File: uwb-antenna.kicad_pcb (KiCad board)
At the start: 2 copper layers, 53 parts, among them J1 USB C, J2 Battery, J3 SWD, SW1 ~{PB}, SW2 BOOT0, SW4 ~{SR}, U1 STM6600, U2 BQ24074RGT, U3 TPS63001, U5 STM32L432KBUx

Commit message: start placing some components in PCB design
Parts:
- removed D6: LTST-C235KGKRKT, LED_SMD:LED_LiteOn_LTST-C235KGKRKT
- removed J3: SWD, Connector_PinHeader_2.54mm:PinHeader_1x04_P2.54mm_Vertical
- added C3: 0.1uF, Capacitor_SMD:C_0402_1005Metric, F.Cu at (91.7, 117.5)
- added D7: LED_Dual_AAKK, LED_SMD:LED_LiteOn_LTST-C295K_1.6x0.8mm, F.Cu at (172.7, 84.5)
- added H1: MH1, MountingHole:MountingHole_3.2mm_M3_Pad, F.Cu at (140.9, 123.9)
- added H2: MH2, MountingHole:MountingHole_3.2mm_M3_Pad, F.Cu at (174.9, 123.9)
- added H3: MH3, MountingHole:MountingHole_3.2mm_M3_Pad, F.Cu at (174.9, 64.9)
- added H4: MH4, MountingHole:MountingHole_3.2mm_M3_Pad, F.Cu at (140.9, 64.9)
- added J4: Conn_ST_STDC14, Connector_PinHeader_1.27mm:PinHeader_2x07_P1.27mm_Vertical_SMD, F.Cu at (173.1, 92.1)
- J2: footprint BH-18650-PC:BAT_BH-18650-PC -> Connector_JST:JST_PH_S2B-PH-SM4-TB_1x02-1MP_P2.00mm_Horizontal
- R17, R6: footprint Resistor_SMD:R_0805_2012Metric -> Resistor_SMD:R_0402_1005Metric
- moved DWM1 58.7 mm to (157.9, 74.7)
- moved D1 56.4 mm to (115.6, 109.4)
- moved R17 53.4 mm to (175.1, 85.0)
- moved R12 53.0 mm to (92.0, 92.6)
- moved R13 53.0 mm to (92.0, 94.6)
- moved R15 53.0 mm to (92.0, 96.6)
- moved R16 53.0 mm to (92.0, 98.6)
- moved U1 53.0 mm to (112.3, 94.0)
- moved C1 53.0 mm to (74.5, 102.6)
- moved C2 53.0 mm to (74.5, 104.6)
- moved C4 53.0 mm to (74.5, 106.5)
- moved C5 53.0 mm to (74.5, 108.5)
- moved C7 53.0 mm to (74.5, 110.5)
- moved D2 53.0 mm to (86.4, 100.6)
- moved D3 53.0 mm to (86.4, 102.6)
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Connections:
- U5 pad 26: /~{CE} -> /SWO
- U5 pad 27: unconnected-(U5-PB4-Pad27) -> /~{CE}
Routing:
- added copper zone on F.Cu, net GND
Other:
- board outline added: 40 x 68 mm

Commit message: feat: place other components in the PCB
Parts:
- added C18: 4.7uF, Capacitor_SMD:C_0805_2012Metric, F.Cu at (166.6, 101.5)
- C7: footprint Capacitor_SMD:C_0402_1005Metric -> Capacitor_SMD:C_0805_2012Metric
- moved C7 88.4 mm to (162.7, 106.4)
- moved R1 83.9 mm to (164.3, 123.1), turned to 90 degrees
- moved R9 77.3 mm to (165.9, 103.1)
- moved R10 77.2 mm to (165.9, 104.4)
- moved R12 75.2 mm to (165.9, 106.4)
- moved R2 71.4 mm to (151.6, 123.1), turned to 90 degrees
- moved R11 70.5 mm to (159.4, 104.0), turned to -90 degrees
- moved U2 67.3 mm to (162.6, 101.7), turned to 180 degrees
- moved C8 63.3 mm to (158.9, 100.7), turned to 90 degrees
- moved FB1 59.9 mm to (154.4, 118.1), turned to 90 degrees
- moved D1 43.1 mm to (157.9, 117.7), turned to -90 degrees
- moved C3 11.5 mm to (84.1, 108.8)
- moved C9 10.8 mm to (164.8, 119.0), turned to 0 degrees
- moved R14 10.5 mm to (162.3, 119.0), turned to 0 degrees
- moved U5 9.16 mm to (144.4, 107.4)
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
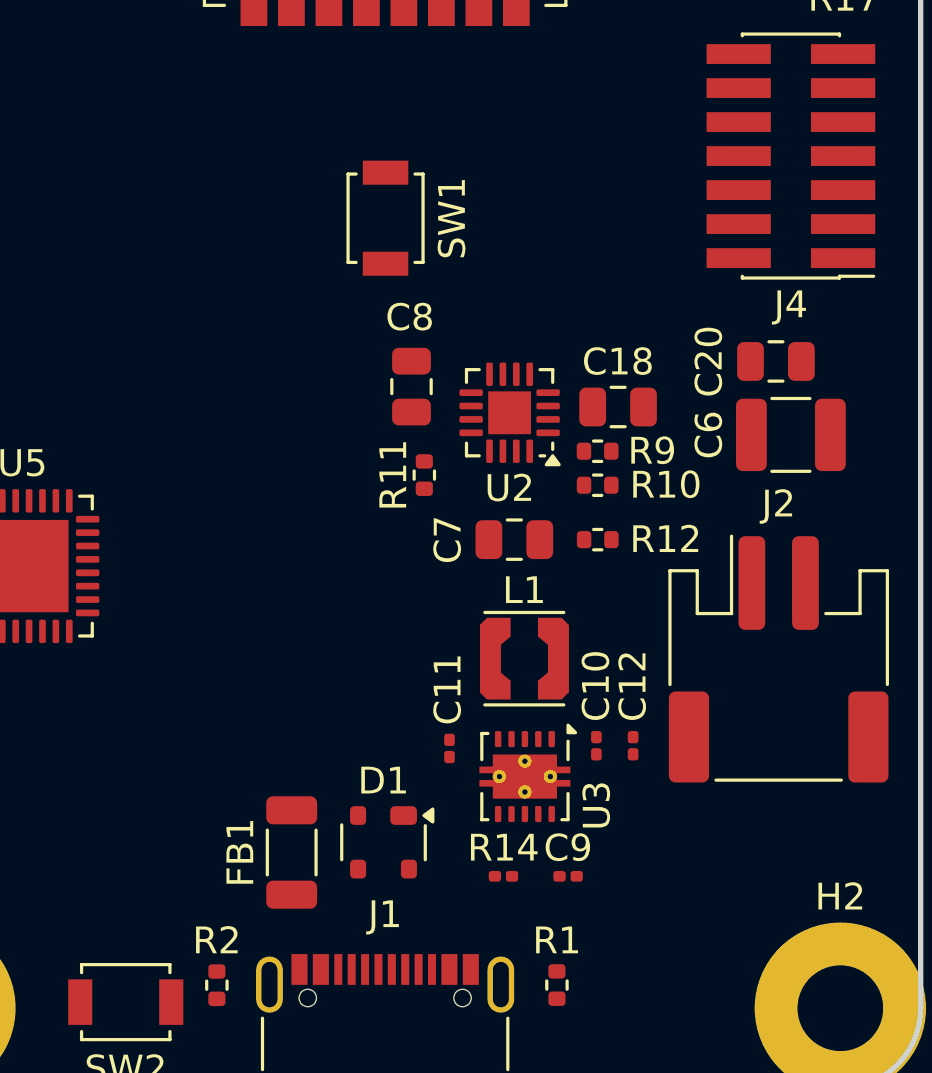
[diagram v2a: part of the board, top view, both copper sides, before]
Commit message: add battery filled zone
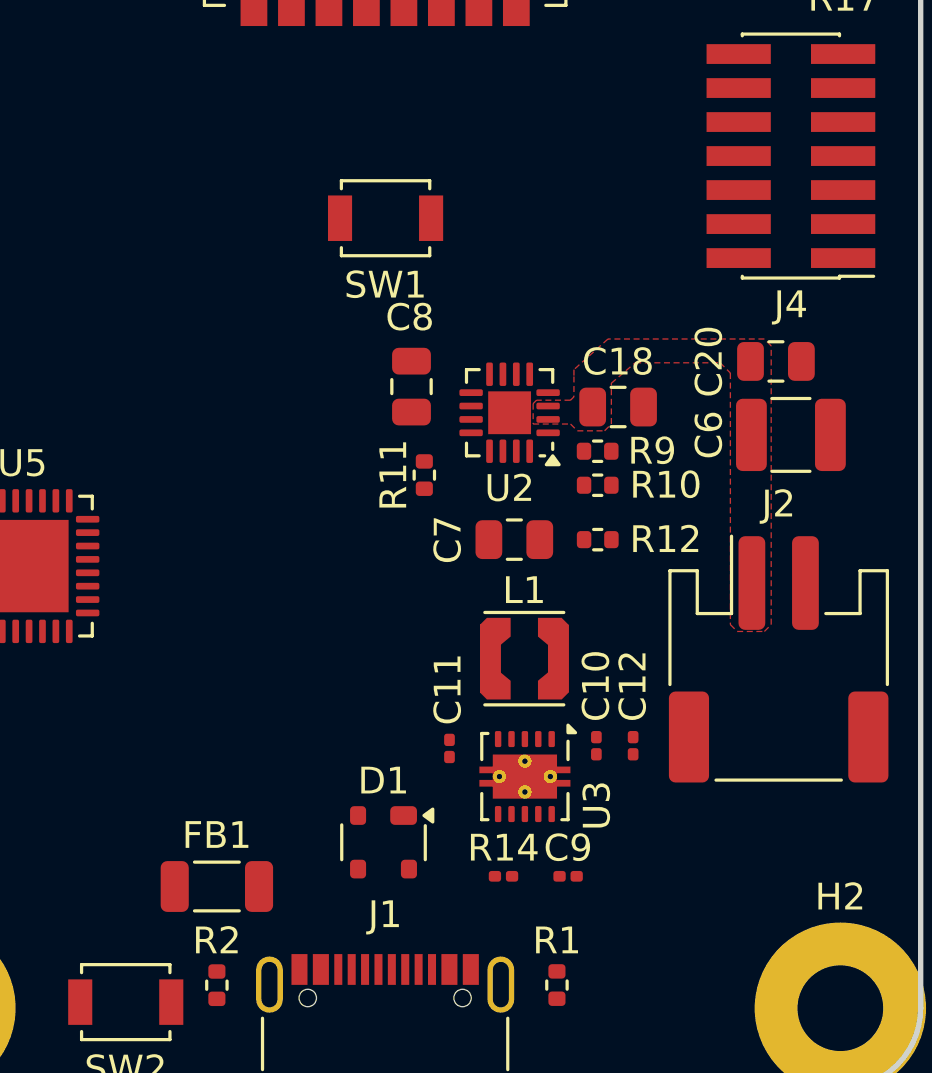
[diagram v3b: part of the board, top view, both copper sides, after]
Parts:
- moved FB1 3.07 mm to (151.6, 119.4), turned to 180 degrees
- turned SW1 to 180 degrees
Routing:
- added copper zone on F.Cu, net /BAT
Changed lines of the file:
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@@
 	(footprint "Inductor_SMD:L_1206_3216Metric"
 		(layer "F.Cu")
-		(at 154.432 118.11 90)
+		(at 151.638 119.38 180)
 		(descr "Inductor SMD 1206 (3216 Metric), square (rectangular) end terminal, IPC-7351 nominal, (Body size source: IPC-SM-782 page 80, https://www.pcb-3d.com/wordpress/wp-content/uploads/ipc-sm-782a_amendment_1_and_2.pdf), generated with kicad-footprint-generator")
 		(tags "inductor")
 		(property "Reference" "FB1"
-			(at 0 -1.9 90)
+			(at 0 1.905 0)
 			(layer "F.SilkS")
 			(effects
@@
 		)
 		(property "Value" "GZ3216D101TF"
-			(at 0 1.9 90)
+			(at 0 1.9 0)
 			(layer "F.Fab")
 			(effects
@@
 		)
 		(property "Datasheet" "~"
-			(at 0 0 90)
+			(at 0 0 0)
 			(layer "F.Fab")
 			(hide yes)
@@
 		)
 		(property "Description" "Ferrite bead, small symbol"
-			(at 0 0 90)
+			(at 0 0 0)
 			(layer "F.Fab")
 			(hide yes)
@@
 		)
 		(property "LCSC" "C369799"
-			(at 0 0 90)
+			(at 0 0 180)
 			(unlocked yes)
 			(layer "F.Fab")
@@
 		(attr smd)
 		(fp_line
-			(start -0.835242 -0.91)
-			(end 0.835242 -0.91)
+			(start -0.835242 0.91)
+			(end 0.835242 0.91)
 			(stroke
 				(width 0.12)
@@
 		)
 		(fp_line
-			(start -0.835242 0.91)
-			(end 0.835242 0.91)
+			(start -0.835242 -0.91)
+			(end 0.835242 -0.91)
 			(stroke
 				(width 0.12)
@@
 		)
 		(fp_line
-			(start 2.35 -1.2)
-			(end 2.35 1.2)
+			(start 2.35 1.2)
+			(end -2.35 1.2)
 			(stroke
 				(width 0.05)
@@
 		)
 		(fp_line
-			(start -2.35 -1.2)
-			(end 2.35 -1.2)
+			(start 2.35 -1.2)
+			(end 2.35 1.2)
 			(stroke
 				(width 0.05)
@@
 		)
 		(fp_line
-			(start 2.35 1.2)
-			(end -2.35 1.2)
+			(start -2.35 1.2)
+			(end -2.35 -1.2)
 			(stroke
 				(width 0.05)
@@
 		)
 		(fp_line
-			(start -2.35 1.2)
-			(end -2.35 -1.2)
+			(start -2.35 -1.2)
+			(end 2.35 -1.2)
 			(stroke
 				(width 0.05)
@@
 		)
 		(fp_line
-			(start 1.6 -0.8)
-			(end 1.6 0.8)
+			(start 1.6 0.8)
+			(end -1.6 0.8)
 			(stroke
 				(width 0.1)
@@
 		)
 		(fp_line
-			(start -1.6 -0.8)
-			(end 1.6 -0.8)
+			(start 1.6 -0.8)
+			(end 1.6 0.8)
 			(stroke
 				(width 0.1)
@@
 		)
 		(fp_line
-			(start 1.6 0.8)
-			(end -1.6 0.8)
+			(start -1.6 0.8)
+			(end -1.6 -0.8)
 			(stroke
 				(width 0.1)
@@
 		)
 		(fp_line
-			(start -1.6 0.8)
-			(end -1.6 -0.8)
+			(start -1.6 -0.8)
+			(end 1.6 -0.8)
 			(stroke
 				(width 0.1)
@@
 		)
 		(fp_text user "${REFERENCE}"
-			(at 0 0 90)
+			(at 0 0 0)
 			(layer "F.Fab")
 			(effects
@@
 		)
 		(pad "1" smd roundrect
-			(at -1.575 0 90)
+			(at -1.575 0 180)
 			(size 1.05 1.9)
 			(layers "F.Cu" "F.Mask" "F.Paste")
@@
 		)
 		(pad "2" smd roundrect
-			(at 1.575 0 90)
+			(at 1.575 0 180)
 			(size 1.05 1.9)
 			(layers "F.Cu" "F.Mask" "F.Paste")
@@
 		(locked yes)
 		(layer "F.Cu")
-		(at 157.9372 94.422399 -90)
+		(at 157.9372 94.422399 180)
 		(descr "Ultra-small-sized Tactile Switch with High Contact Reliability, Top-actuated Model, without Ground Terminal, without Boss")
 		(tags "Tactile Switch")
 		(property "Reference" "SW1"
-			(at 0 -2.5 90)
+			(at 0 -2.5 0)
 			(layer "F.SilkS")
 			(effects
@@
 		)
 		(property "Value" "~{PB}"
-			(at 0 2.5 90)
+			(at 0 2.5 0)
 			(layer "F.Fab")
 			(effects
@@
 		)
 		(property "Datasheet" "~"
-			(at 0 0 270)
+			(at 0 0 180)
 			(unlocked yes)
 			(layer "F.Fab")
@@
 		)
 		(property "Description" "Push button switch, generic, two pins"
-			(at 0 0 270)
+			(at 0 0 180)
 			(unlocked yes)
 			(layer "F.Fab")
@@
 		)
 		(property "LCSC" "C231329"
-			(at 0 0 270)
+			(at 0 0 180)
 			(unlocked yes)
 			(layer "F.Fab")
@@
 		(attr smd)
 		(fp_line
-			(start -1.65 1.4)
-			(end 1.65 1.4)
+			(start 1.65 1.4)
+			(end 1.65 1.1)
 			(stroke
 				(width 0.12)
@@
 		)
 		(fp_line
-			(start 1.65 1.4)
-			(end 1.65 1.1)
+			(start 1.65 -1.4)
+			(end 1.65 -1.1)
 			(stroke
 				(width 0.12)
@@
 		)
 		(fp_line
-			(start -1.65 1.1)
-			(end -1.65 1.4)
+			(start -1.65 1.4)
+			(end 1.65 1.4)
 			(stroke
 				(width 0.12)
@@
 		)
 		(fp_line
-			(start -1.65 -1.1)
-			(end -1.65 -1.4)
+			(start -1.65 1.1)
+			(end -1.65 1.4)
 			(stroke
 				(width 0.12)
@@
 		)
 		(fp_line
-			(start -1.65 -1.4)
-			(end 1.65 -1.4)
+			(start -1.65 -1.1)
+			(end -1.65 -1.4)
 			(stroke
 				(width 0.12)
@@
 		)
 		(fp_line
-			(start 1.65 -1.4)
-			(end 1.65 -1.1)
+			(start -1.65 -1.4)
+			(end 1.65 -1.4)
 			(stroke
 				(width 0.12)
@@
 		)
 		(fp_line
-			(start -2.4 1.65)
-			(end 2.4 1.65)
+			(start 2.4 1.65)
+			(end 2.4 -1.65)
 			(stroke
 				(width 0.05)
@@
 		)
 		(fp_line
-			(start 2.4 1.65)
-			(end 2.4 -1.65)
+			(start 2.4 -1.65)
+			(end -2.4 -1.65)
 			(stroke
 				(width 0.05)
@@
 		)
 		(fp_line
-			(start -2.4 -1.65)
-			(end -2.4 1.65)
+			(start -2.4 1.65)
+			(end 2.4 1.65)
 			(stroke
 				(width 0.05)
@@
 		)
 		(fp_line
-			(start 2.4 -1.65)
-			(end -2.4 -1.65)
+			(start -2.4 -1.65)
+			(end -2.4 1.65)
 			(stroke
 				(width 0.05)
@@
 		)
 		(fp_line
-			(start -1.5 1.25)
-			(end -1.5 -1.25)
+			(start 1.5 1.25)
+			(end -1.5 1.25)
 			(stroke
 				(width 0.1)
@@
 		)
 		(fp_line
-			(start 1.5 1.25)
-			(end -1.5 1.25)
+			(start 1.5 -1.25)
+			(end 1.5 1.25)
 			(stroke
 				(width 0.1)
@@
 		)
 		(fp_line
-			(start -1.5 -1.25)
-			(end 1.5 -1.25)
+			(start -1.5 1.25)
+			(end -1.5 -1.25)
 			(stroke
 				(width 0.1)
@@
 		)
 		(fp_line
-			(start 1.5 -1.25)
-			(end 1.5 1.25)
+			(start -1.5 -1.25)
+			(end 1.5 -1.25)
 			(stroke
 				(width 0.1)
@@
 		)
 		(fp_text user "${REFERENCE}"
-			(at 0 -2.5 90)
+			(at 0 -2.5 0)
 			(layer "F.Fab")
 			(effects
@@
 		)
 		(pad "1" smd rect
-			(at -1.7 0 270)
+			(at -1.7 0 180)
 			(size 0.9 1.7)
 			(layers "F.Cu" "F.Mask" "F.Paste")
@@
 		)
 		(pad "2" smd rect
-			(at 1.7 0 270)
+			(at 1.7 0 180)
 			(size 0.9 1.7)
 			(layers "F.Cu" "F.Mask" "F.Paste")
@@
 	)
 	(zone
+		(net 5)
+		(net_name "/BAT")
+		(layer "F.Cu")
+		(hatch edge 0.5)
+		(priority 1)
+		(connect_pads yes
+			(clearance 0)
+		)
+		(min_thickness 0.25)
+		(filled_areas_thickness no)
+		(fill yes
+			(thermal_gap 0.5)
+			(thermal_bridge_width 0.5)
+		)
+		(polygon
+			(pts
+				(xy 163.449 102.108) (xy 164.846 102.108) (xy 165.1 102.362) (xy 166.116 102.362) (xy 166.37 102.108)
+				(xy 166.37 100.584) (xy 167.259 99.822) (xy 170.434 99.822) (xy 170.815 100.203) (xy 170.815 109.601)
+				(xy 171.069 109.855) (xy 172.085 109.855) (xy 172.339 109.601) (xy 172.339 99.187) (xy 172.085 98.933)
+				(xy 166.243 98.933) (xy 164.973 100.076) (xy 164.973 100.076) (xy 164.973 100.33) (xy 164.973 101.092)
+				(xy 164.846 101.219) (xy 163.576 101.219) (xy 163.449 101.346)
+			)
+		)
+	)
+	(zone
 		(net 1)
 		(net_name "GND")
@@
 		(name "L2")
 		(hatch edge 0.1)
-		(priority 1)
 		(connect_pads
 			(clearance 0.01)
@@
 			(thermal_gap 0.5)
 			(thermal_bridge_width 0.5)
+			(island_removal_mode 1)
+			(island_area_min 10)
 		)
 		(polygon

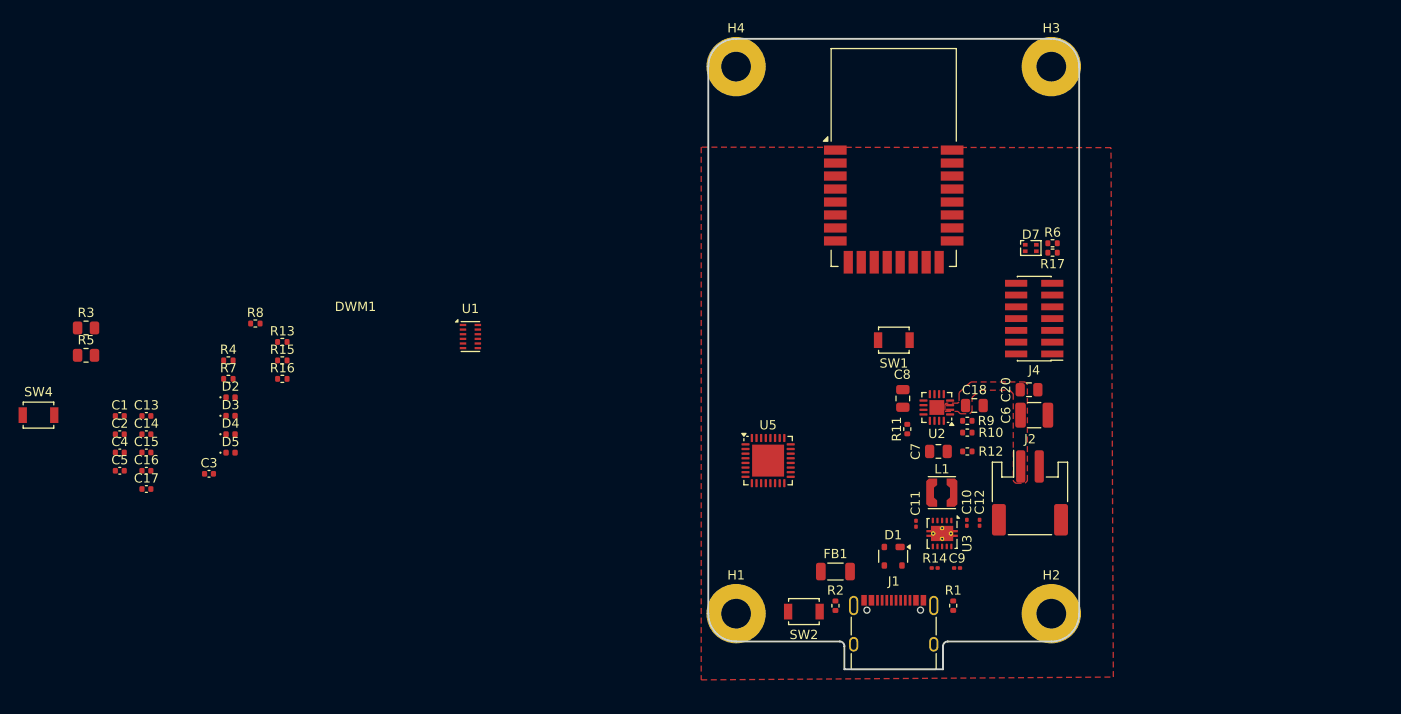
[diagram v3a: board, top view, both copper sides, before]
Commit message: add some traces
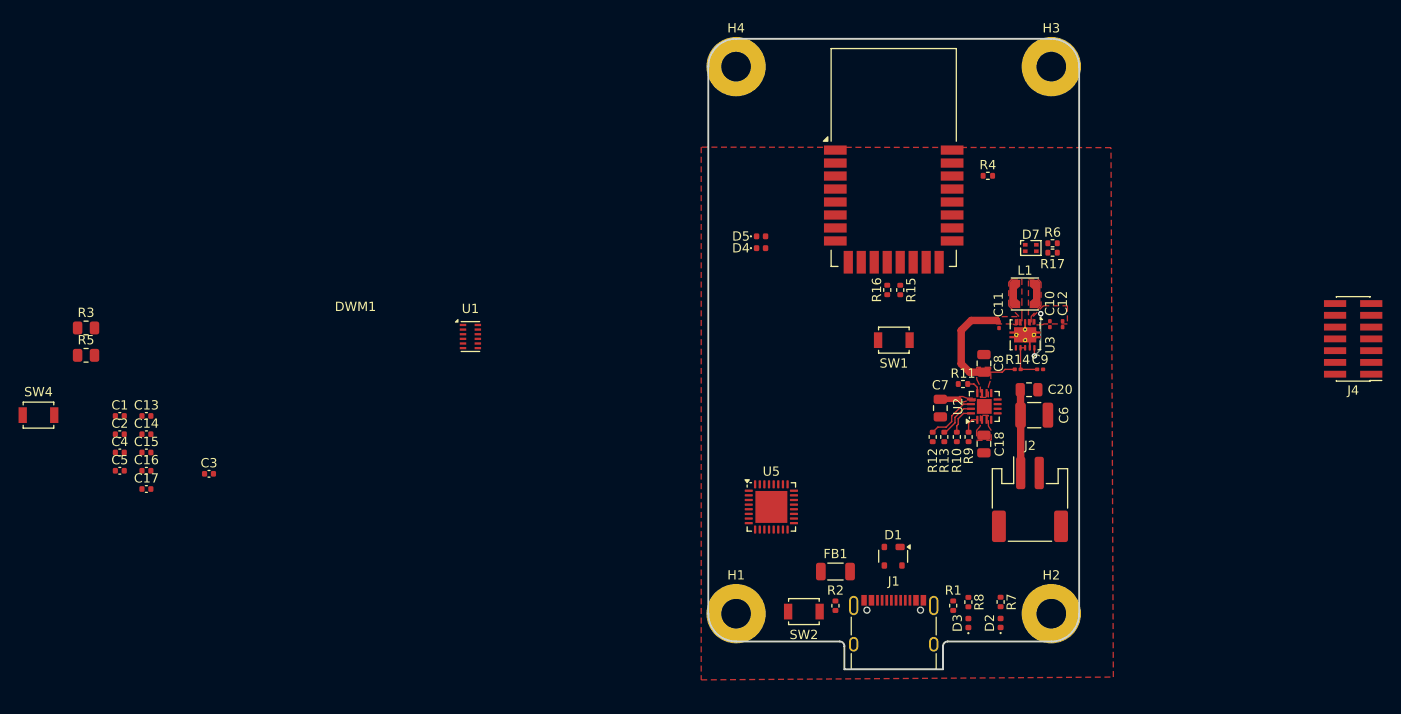
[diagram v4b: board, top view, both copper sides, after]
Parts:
- moved R7 86.7 mm to (169.4, 122.7), turned to -90 degrees
- moved D2 86.5 mm to (169.4, 124.9), turned to 90 degrees
- moved R4 84.3 mm to (168.1, 76.7)
- moved D3 82.7 mm to (166.0, 124.9), turned to 90 degrees
- moved R8 82.6 mm to (166.0, 122.7), turned to -90 degrees
- moved R13 72.1 mm to (163.4, 104.9), turned to -90 degrees
- moved R15 67.1 mm to (158.6, 89.0), turned to -90 degrees
- moved R16 65.9 mm to (157.2, 89.0), turned to -90 degrees
- moved D5 61.8 mm to (143.6, 83.2)
- moved D4 60.6 mm to (143.6, 84.5)
- moved J4 34.5 mm to (207.5, 94.3)
- moved C12 23.2 mm to (176.1, 92.7)
- moved U3 23.2 mm to (172.1, 93.8)
- moved C10 23.2 mm to (174.8, 92.7)
- moved C9 23.2 mm to (173.7, 97.6)
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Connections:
- C10 pad 1: +3V3 -> +3.3V
- C12 pad 1: +3V3 -> +3.3V
- U3 pad 1: +3V3 -> +3.3V
- U3 pad 10: +3V3 -> +3.3V
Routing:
- net /BATT_OUT: track 0.00 -> 14.1 mm
- net /BAT: track 0.00 -> 9.00 mm
- net Net-(U2-TMR): track 0.00 -> 5.73 mm
- net +3.3V: track 0.00 -> 5.72 mm, vias 0 -> 2
- net Net-(U3-PS/SYNC): track 0.00 -> 4.61 mm
- net Net-(U2-ITERM): track 0.00 -> 4.28 mm
- net Net-(U2-ISET): track 0.00 -> 3.13 mm
- net GND: track 0.00 -> 2.43 mm
- net Net-(U2-TS): track 0.00 -> 2.07 mm
- net VBUS: track 0.00 -> 2.02 mm
- net Net-(U2-ILIM): track 0.00 -> 1.81 mm
- added copper zone on F.Cu, net +3.3V
- added copper zone on F.Cu, net /BATT_OUT
- added copper zone on F.Cu, net Net-(U3-L1)
- added copper zone on F.Cu, net Net-(U3-L2)
- added copper zone on F.Cu, net VBUS

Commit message: complete PCB design
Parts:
- removed C16, C17: 0.1uF, Capacitor_SMD:C_0402_1005Metric
- removed D1: SP0503BAHT, Package_TO_SOT_SMD:SOT-143
- removed H2: MH2, MountingHole:MountingHole_3.2mm_M3_Pad
- removed J4: Conn_ST_STDC14, Connector_PinHeader_1.27mm:PinHeader_2x07_P1.27mm_Vertical_SMD
- removed R3: 0, Resistor_SMD:R_0805_2012Metric
- added J3: TC2030-NL, Connector:Tag-Connect_TC2030-IDC-NL_2x03_P1.27mm_Vertical, F.Cu at (127.9, 90.1)
- added U4: TPD2EUSB30, Package_TO_SOT_SMD:Texas_DRT-3, F.Cu at (139.2, 119.1)
- C10, C11, C12: footprint Capacitor_SMD:C_0201_0603Metric -> Capacitor_SMD:C_0603_1608Metric
- C15: value 0.1uF -> 560nF
- R5: footprint Resistor_SMD:R_0805_2012Metric -> Resistor_SMD:R_0402_1005Metric
- moved SW4 70.1 mm to (134.5, 115.8), turned to 90 degrees
- moved R5 63.2 mm to (129.6, 119.3), turned to -90 degrees
- moved C4 59.5 mm to (129.8, 84.7), turned to 180 degrees
- moved C1 56.7 mm to (131.1, 99.2), turned to -90 degrees
- moved C14 56.5 mm to (133.5, 110.6), turned to -90 degrees
- moved C2 55.4 mm to (129.8, 100.8)
- moved R4 54.7 mm to (126.0, 111.7), turned to -90 degrees
- moved C15 52.0 mm to (128.2, 95.8), turned to 180 degrees
- moved C5 50.7 mm to (125.2, 108.0), turned to 180 degrees
- moved C13 50.1 mm to (127.4, 103.6), turned to 90 degrees
- moved C3 41.2 mm to (125.2, 107.0), turned to 180 degrees
- moved H3 29.4 mm to (150.2, 80.7), turned to 180 degrees
- moved D2 28.9 mm to (149.5, 104.0), turned to 0 degrees
- moved D3 28.5 mm to (149.5, 101.7), turned to 0 degrees
- moved C9 27.2 mm to (146.8, 101.2)
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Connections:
- C15 pad 1: +3.3V -> Net-(U1-C_SRD)
- J1 pad S1: Net-(J1-SHIELD) -> GND
- U1 pad 5: unconnected-(U1-C_SRD-Pad5) -> Net-(U1-C_SRD)
- U5 pad 18: /LED_G -> /LED_R
- U5 pad 19: /LED_R -> /LED_G
- U5 pad 2: unconnected-(U5-PC14-Pad2) -> /UWB_RST
- U5 pad 20: unconnected-(U5-PA10-Pad20) -> /~{CE}
- U5 pad 27: /~{CE} -> unconnected-(U5-PB4-Pad27)
- U5 pad 3: unconnected-(U5-PC15-Pad3) -> /WAKEUP
- U5 pad 6: /UWB_RST -> unconnected-(U5-PA0-Pad6)
- U5 pad 7: /WAKEUP -> unconnected-(U5-PA1-Pad7)
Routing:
- net +3.3V: track 5.72 -> 90.4 mm, vias 2 -> 10
- net /IRQ: track 0.00 -> 51.2 mm, vias 0 -> 2
- net /CS: track 0.00 -> 41.5 mm, vias 0 -> 2
- net /CLK: track 0.00 -> 41.4 mm, vias 0 -> 2
- net /MISO: track 0.00 -> 40.2 mm, vias 0 -> 2
- net /WAKEUP: track 0.00 -> 40.0 mm, vias 0 -> 2
- net /LED_G: track 0.00 -> 39.3 mm, vias 0 -> 2
- net /MOSI: track 0.00 -> 39.1 mm, vias 0 -> 2
- net /UWB_RST: track 0.00 -> 38.8 mm, vias 0 -> 2
- net /LED_R: track 0.00 -> 38.5 mm, vias 0 -> 2
- net /EN: track 0.00 -> 28.9 mm, vias 0 -> 2
- net /BATT_OUT: track 14.1 -> 39.9 mm
- net /NRST: track 0.00 -> 24.0 mm
- net /D+: track 0.00 -> 23.9 mm
- net /D-: track 0.00 -> 22.2 mm
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- added copper zone on B.Cu, net +3.3V
- added copper zone on B.Cu, net GND
- added copper zone on F.Cu, net Net-(FB1-Pad1)
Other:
- board size 40 x 68 mm -> 30 x 57 mm
